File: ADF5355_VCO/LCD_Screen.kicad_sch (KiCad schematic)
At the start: 3 parts

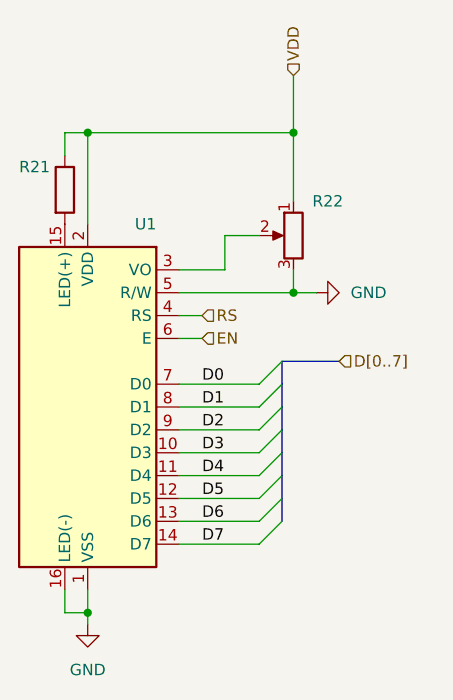
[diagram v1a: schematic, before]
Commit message: Changed the power port
Changed all power ports to be global instead of them being hierarchical sheet pins
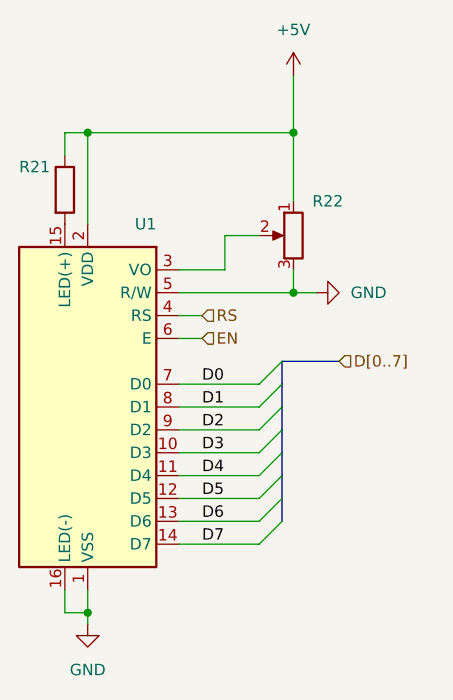
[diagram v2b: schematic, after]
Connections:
- net VDD renamed +5V
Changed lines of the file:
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@@
     (effects (font (size 1.27 1.27)) (justify left bottom))
-  )
-  (hierarchical_label "VDD" (shape input) (at 143.51 55.88 90) (fields_autoplaced)
-    (effects (font (size 1.27 1.27)) (justify left))
   )
   (hierarchical_label "D[0..7]" (shape input) (at 148.59 87.63 0) (fields_autoplaced)
@@
         )
       )
+    )
+  )
+  (symbol (lib_id "power:+5V") (at 143.51 55.88 0) (unit 1)
+    (in_bom yes) (on_board yes) (dnp no) (fields_autoplaced)
+    (property "Reference" "#PWR040" (at 143.51 59.69 0)
+      (effects (font (size 1.27 1.27)) hide)
+    )
+    (property "Value" "+5V" (at 143.51 50.8 0)
+      (effects (font (size 1.27 1.27)))
+    )
+    (property "Footprint" "" (at 143.51 55.88 0)
+      (effects (font (size 1.27 1.27)) hide)
+    )
+    (property "Datasheet" "" (at 143.51 55.88 0)
+      (effects (font (size 1.27 1.27)) hide)
+    )
+    (pin "1")
+    (instances
+      (project "ADF5355_VCO"
+        (path "/29349b68-071c-451b-9b1e-10b5ef7e12a6/fa8fa127-05a9-4ec7-8a64-8bfb966dae3d"
+          (reference "#PWR040") (unit 1)
+        )
+      )

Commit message: Added footprints to some components
Footprints added for:
SMA connectors
DC banana connector
USB connector
LCD screen
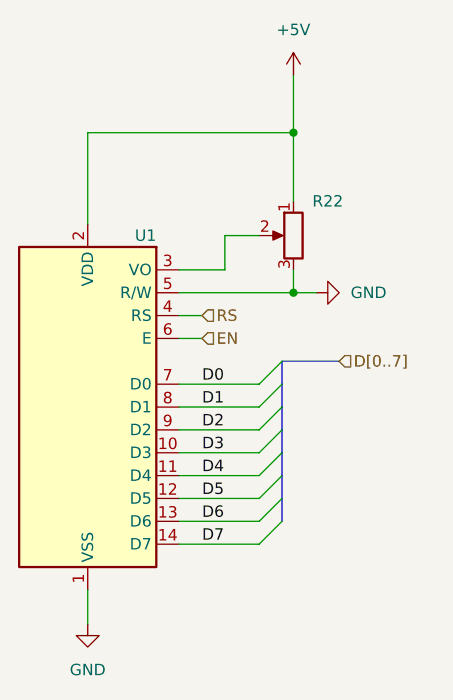
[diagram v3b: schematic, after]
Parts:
- removed R21: R, symbol Device:R
- U1: footprint (none) -> ADF5355_footprint_lib:162K-CC_BC-3LP
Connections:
- net GND: no longer U1.16 (LED(-))
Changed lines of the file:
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@@
 (kicad_sch (version 20230121) (generator eeschema)
   (paper "A4")
-  (junction (at 120.65 62.23) (diameter 0) (color 0 0 0 0)
-  )
   (junction (at 143.51 62.23) (diameter 0) (color 0 0 0 0)
   )
   (junction (at 143.51 80.01) (diameter 0) (color 0 0 0 0)
   )
-  (junction (at 120.65 115.57) (diameter 0) (color 0 0 0 0)
-  )
   (bus_entry (at 139.7 102.87) (size 2.54 -2.54)
     (stroke (width 0) (type default))
@@
     (stroke (width 0) (type default))
   )
-  (wire (pts (xy 120.65 116.84) (xy 120.65 115.57))
-    (stroke (width 0) (type default))
-  )
   (bus (pts (xy 142.24 90.17) (xy 142.24 92.71))
     (stroke (width 0) (type default))
@@
     (stroke (width 0) (type default))
   )
-  (wire (pts (xy 118.11 64.77) (xy 118.11 62.23))
-    (stroke (width 0) (type default))
-  )
-  (wire (pts (xy 118.11 115.57) (xy 120.65 115.57))
-    (stroke (width 0) (type default))
-  )
-  (wire (pts (xy 118.11 62.23) (xy 120.65 62.23))
-    (stroke (width 0) (type default))
-  )
   (wire (pts (xy 130.81 107.95) (xy 139.7 107.95))
     (stroke (width 0) (type default))
@@
     (stroke (width 0) (type default))
   )
-  (wire (pts (xy 120.65 115.57) (xy 120.65 113.03))
+  (wire (pts (xy 120.65 113.03) (xy 120.65 116.84))
     (stroke (width 0) (type default))
   )
@@
   )
   (wire (pts (xy 143.51 80.01) (xy 146.05 80.01))
-    (stroke (width 0) (type default))
-  )
-  (wire (pts (xy 118.11 113.03) (xy 118.11 115.57))
     (stroke (width 0) (type default))
   )
@@
     (effects (font (size 1.27 1.27)) (justify left))
   )
-  (symbol (lib_id "power:GND") (at 120.65 116.84 0) (unit 1)
-    (in_bom yes) (on_board yes) (dnp no) (fields_autoplaced)
-    (property "Reference" "#PWR010" (at 120.65 123.19 0)
-      (effects (font (size 1.27 1.27)) hide)
-    )
-    (property "Value" "GND" (at 120.65 121.92 0)
-      (effects (font (size 1.27 1.27)))
-    )
-    (property "Footprint" "" (at 120.65 116.84 0)
-      (effects (font (size 1.27 1.27)) hide)
-    )
-    (property "Datasheet" "" (at 120.65 116.84 0)
-      (effects (font (size 1.27 1.27)) hide)
-    )
-    (pin "1")
-    (instances
-      (project "ADF5355_VCO"
-        (path "/29349b68-071c-451b-9b1e-10b5ef7e12a6"
-          (reference "#PWR010") (unit 1)
-        )
-        (path "/29349b68-071c-451b-9b1e-10b5ef7e12a6/fa8fa127-05a9-4ec7-8a64-8bfb966dae3d"
-          (reference "#PWR010") (unit 1)
-        )
-      )
-    )
-  )
-  (symbol (lib_id "power:GND") (at 146.05 80.01 90) (unit 1)
-    (in_bom yes) (on_board yes) (dnp no) (fields_autoplaced)
-    (property "Reference" "#PWR025" (at 152.4 80.01 0)
-      (effects (font (size 1.27 1.27)) hide)
-    )
-    (property "Value" "GND" (at 149.86 80.01 90)
-      (effects (font (size 1.27 1.27)) (justify right))
-    )
-    (property "Footprint" "" (at 146.05 80.01 0)
-      (effects (font (size 1.27 1.27)) hide)
-    )
-    (property "Datasheet" "" (at 146.05 80.01 0)
-      (effects (font (size 1.27 1.27)) hide)
-    )
-    (pin "1")
-    (instances
-      (project "ADF5355_VCO"
-        (path "/29349b68-071c-451b-9b1e-10b5ef7e12a6"
-          (reference "#PWR025") (unit 1)
-        )
-        (path "/29349b68-071c-451b-9b1e-10b5ef7e12a6/fa8fa127-05a9-4ec7-8a64-8bfb966dae3d"
-          (reference "#PWR025") (unit 1)
-        )
-      )
-    )
-  )
   (symbol (lib_id "ADF_5355_Lib:LCD_16x2") (at 120.65 93.98 0) (mirror y) (unit 1)
     (in_bom yes) (on_board yes) (dnp no)
-    (property "Reference" "U1" (at 128.27 72.39 0)
+    (property "Reference" "U1" (at 128.27 73.66 0)
       (effects (font (size 1.27 1.27)) (justify left))
     )
@@
       (effects (font (size 1.27 1.27)))
     )
-    (property "Footprint" "" (at 132.08 91.44 0)
-      (effects (font (size 1.27 1.27)) hide)
-    )
-    (property "Datasheet" "" (at 132.08 91.44 0)
+    (property "Footprint" "ADF5355_footprint_lib:162K-CC_BC-3LP" (at 132.08 91.44 0)
+      (effects (font (size 1.27 1.27)) hide)
+    )
+    (property "Datasheet" "https://hr.mouser.com/datasheet/2/1015/162K-CC-BC-3LP-Displaytech-Spec-1664844.pdf" (at 132.08 91.44 0)
       (effects (font (size 1.27 1.27)) hide)
     )
@@
     (pin "13")
     (pin "14")
-    (pin "15")
-    (pin "16")
     (pin "2")
     (pin "3")
@@
     (instances
       (project "ADF5355_VCO"
-        (path "/29349b68-071c-451b-9b1e-10b5ef7e12a6"
-          (reference "U1") (unit 1)
-        )
         (path "/29349b68-071c-451b-9b1e-10b5ef7e12a6/fa8fa127-05a9-4ec7-8a64-8bfb966dae3d"
           (reference "U1") (unit 1)
@@
     )
   )
-  (symbol (lib_id "Device:R") (at 118.11 68.58 0) (unit 1)
-    (in_bom yes) (on_board yes) (dnp no)
-    (property "Reference" "R21" (at 113.03 66.04 0)
-      (effects (font (size 1.27 1.27)) (justify left))
-    )
-    (property "Value" "R" (at 120.65 69.85 0)
-      (effects (font (size 1.27 1.27)) (justify left) hide)
-    )
-    (property "Footprint" "" (at 116.332 68.58 90)
-      (effects (font (size 1.27 1.27)) hide)
-    )
-    (property "Datasheet" "~" (at 118.11 68.58 0)
+  (symbol (lib_id "power:GND") (at 120.65 116.84 0) (unit 1)
+    (in_bom yes) (on_board yes) (dnp no) (fields_autoplaced)
+    (property "Reference" "#PWR010" (at 120.65 123.19 0)
+      (effects (font (size 1.27 1.27)) hide)
+    )
+    (property "Value" "GND" (at 120.65 121.92 0)
+      (effects (font (size 1.27 1.27)))
+    )
+    (property "Footprint" "" (at 120.65 116.84 0)
+      (effects (font (size 1.27 1.27)) hide)
+    )
+    (property "Datasheet" "" (at 120.65 116.84 0)
       (effects (font (size 1.27 1.27)) hide)
     )
     (pin "1")
-    (pin "2")
     (instances
       (project "ADF5355_VCO"
         (path "/29349b68-071c-451b-9b1e-10b5ef7e12a6"
-          (reference "R21") (unit 1)
+          (reference "#PWR010") (unit 1)
         )
         (path "/29349b68-071c-451b-9b1e-10b5ef7e12a6/fa8fa127-05a9-4ec7-8a64-8bfb966dae3d"
-          (reference "R8") (unit 1)
+          (reference "#PWR010") (unit 1)
         )
       )
+    )
+  )
+  (symbol (lib_id "power:GND") (at 146.05 80.01 90) (unit 1)
+    (in_bom yes) (on_board yes) (dnp no) (fields_autoplaced)
+    (property "Reference" "#PWR025" (at 152.4 80.01 0)
+      (effects (font (size 1.27 1.27)) hide)
+    )
+    (property "Value" "GND" (at 149.86 80.01 90)
+      (effects (font (size 1.27 1.27)) (justify right))
+    )
+    (property "Footprint" "" (at 146.05 80.01 0)
+      (effects (font (size 1.27 1.27)) hide)
+    )
+    (property "Datasheet" "" (at 146.05 80.01 0)
+      (effects (font (size 1.27 1.27)) hide)
+    )
+    (pin "1")
+    (instances
+      (project "ADF5355_VCO"
+        (path "/29349b68-071c-451b-9b1e-10b5ef7e12a6"
+          (reference "#PWR025") (unit 1)
+        )
+        (path "/29349b68-071c-451b-9b1e-10b5ef7e12a6/fa8fa127-05a9-4ec7-8a64-8bfb966dae3d"
+          (reference "#PWR025") (unit 1)
+        )
+      )

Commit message: Added additional footprints and BOM
Added a bill of materials with most of the components.
Added footprints for more components
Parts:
- R22: footprint (none) -> Resistor_SMD:R_0603_1608Metric_Pad0.98x0.95mm_HandSolder
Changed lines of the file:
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@@
       (effects (font (size 1.27 1.27)) hide)
     )
-    (property "Footprint" "" (at 143.51 73.66 0)
+    (property "Footprint" "Resistor_SMD:R_0603_1608Metric_Pad0.98x0.95mm_HandSolder" (at 143.51 73.66 0)
       (effects (font (size 1.27 1.27)) hide)
     )

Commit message: Added TCXO and remaining footprints
Added remaining footprints
    NX3225GD
    710X toggle switch
    SMT button

Added ClearClock AX3 TCXO symbol and footprint

Added TCXO schematic with 3 options:
    LVPECL, LVDS and HCSL
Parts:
- R22: footprint Resistor_SMD:R_0603_1608Metric_Pad0.98x0.95mm_HandSolder -> Potentiometer_THT:Potentiometer_ACP_CA9-V10_Vertical
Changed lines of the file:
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@@
       (effects (font (size 1.27 1.27)) hide)
     )
-    (property "Footprint" "Resistor_SMD:R_0603_1608Metric_Pad0.98x0.95mm_HandSolder" (at 143.51 73.66 0)
+    (property "Footprint" "Potentiometer_THT:Potentiometer_ACP_CA9-V10_Vertical" (at 143.51 73.66 0)
       (effects (font (size 1.27 1.27)) hide)
     )
